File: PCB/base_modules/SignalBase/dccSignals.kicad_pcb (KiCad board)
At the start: 2 copper layers, 48 x 57.5 mm, 17 parts, among them J1 Screw_Terminal_01x02, J3 leds, J4 leds, J5 leds, J6 leds, SW1 SW_SPST, U1 ULN2003A, U2 ULN2003A

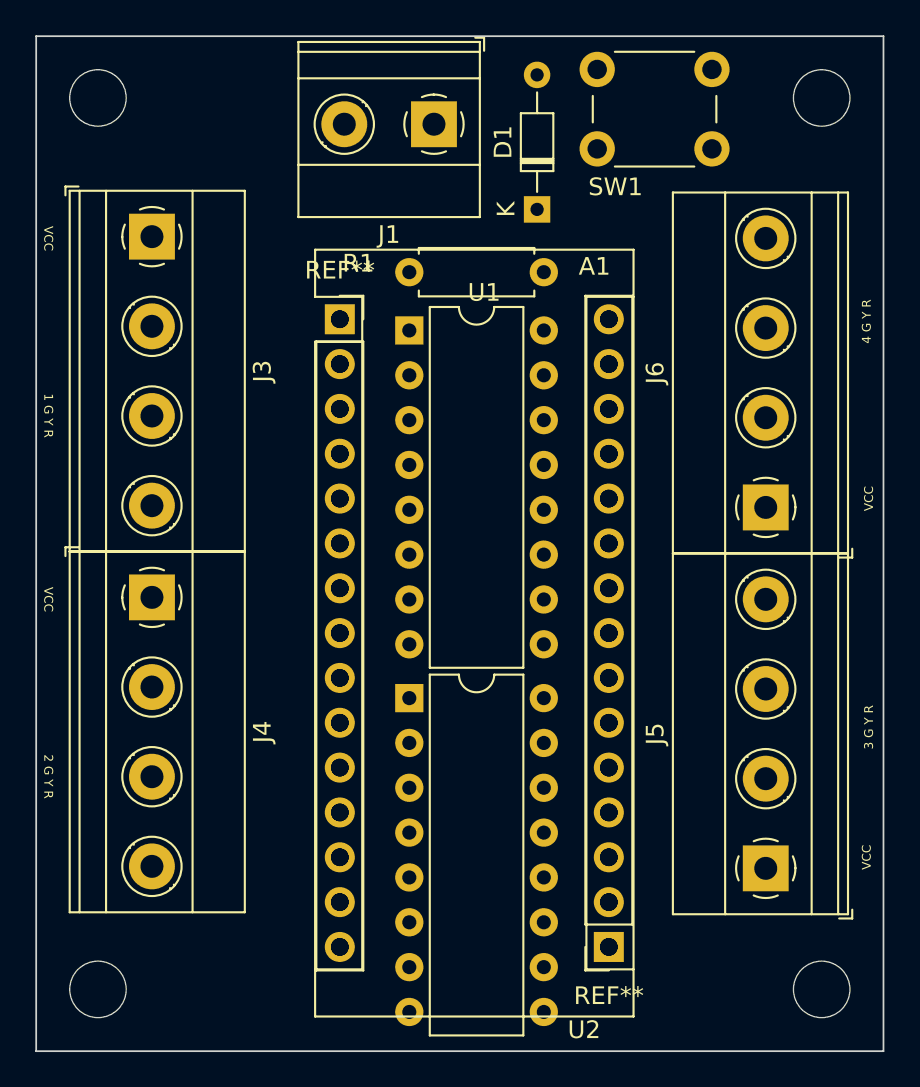
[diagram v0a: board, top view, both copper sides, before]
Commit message: routed signals PCB.
Was thinking to make a loconet block unit. Combined feedback, as well as
signal and ABC module. This would allow for automatic analog block
system for digital trains.
Also was thinking to make 2 separate blocks on 1 one pcb, provided if possible
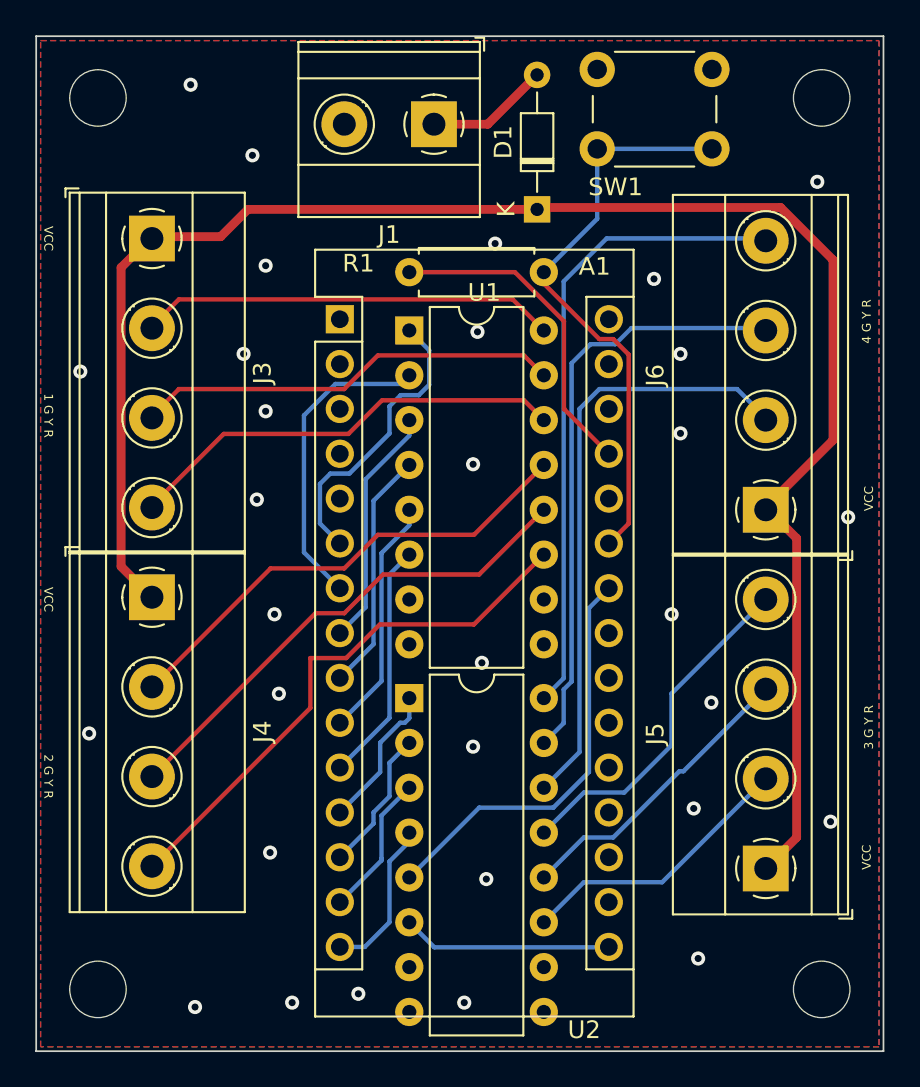
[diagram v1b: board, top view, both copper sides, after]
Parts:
- removed the REF** at (99.4, 133.1)
- removed the REF** at (84.2, 97.5)
- moved J6 0.14 mm to (108.3, 108.3)
- moved J3 0.11 mm to (73.6, 93.0)
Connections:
- U1 pad 9: VCC -> Net-(U1-Pad9)
- U2 pad 9: VCC -> Net-(U2-Pad9)
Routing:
- net VCC: track 0.00 -> 99.9 mm
- net /S4R: track 0.00 -> 36.5 mm
- net /S4G: track 0.00 -> 34.0 mm
- net /S4Y: track 0.00 -> 34.0 mm
- net Net-(A1-Pad25): track 0.00 -> 33.0 mm
- net /S2R: track 0.00 -> 31.2 mm
- net /S2Y: track 0.00 -> 28.5 mm
- net /S2G: track 0.00 -> 27.4 mm
- net /S1R: track 0.00 -> 25.1 mm
- net /S1Y: track 0.00 -> 24.1 mm
- net /S1G: track 0.00 -> 23.6 mm
- net /S3Y_IN: track 0.00 -> 23.5 mm
- net /S3R: track 0.00 -> 19.8 mm
- net +5V: track 0.00 -> 18.5 mm
- net /S1Y_IN: track 0.00 -> 17.5 mm
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- added copper zone on B.Cu, net GND
- added copper zone on F.Cu, net GND

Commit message: added detector pcb and signal pcb
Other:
- board text added: "V+"
- board text added: "V-"

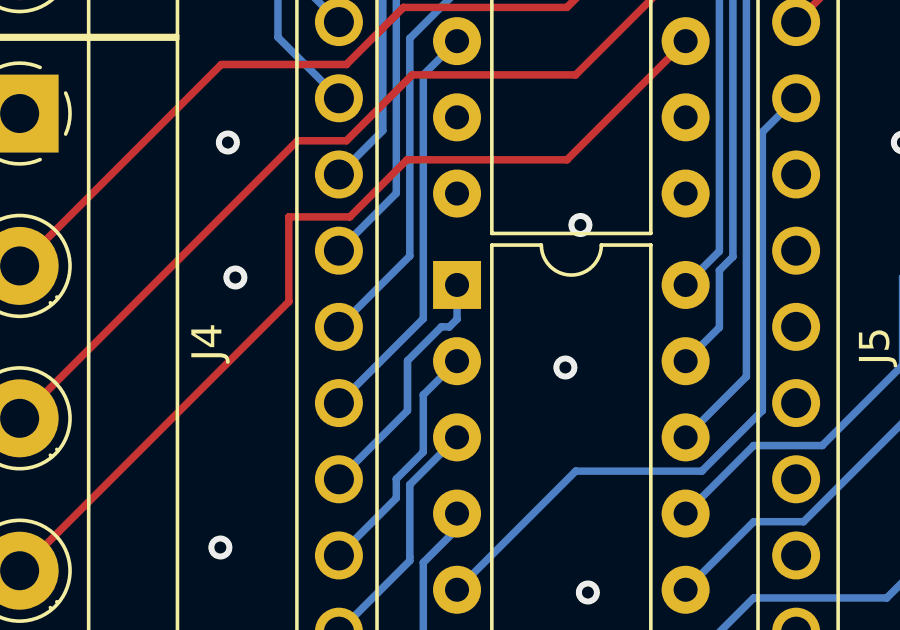
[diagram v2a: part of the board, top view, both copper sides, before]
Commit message: added gerber files in the release folder for all base units. The interfaces are not yet done
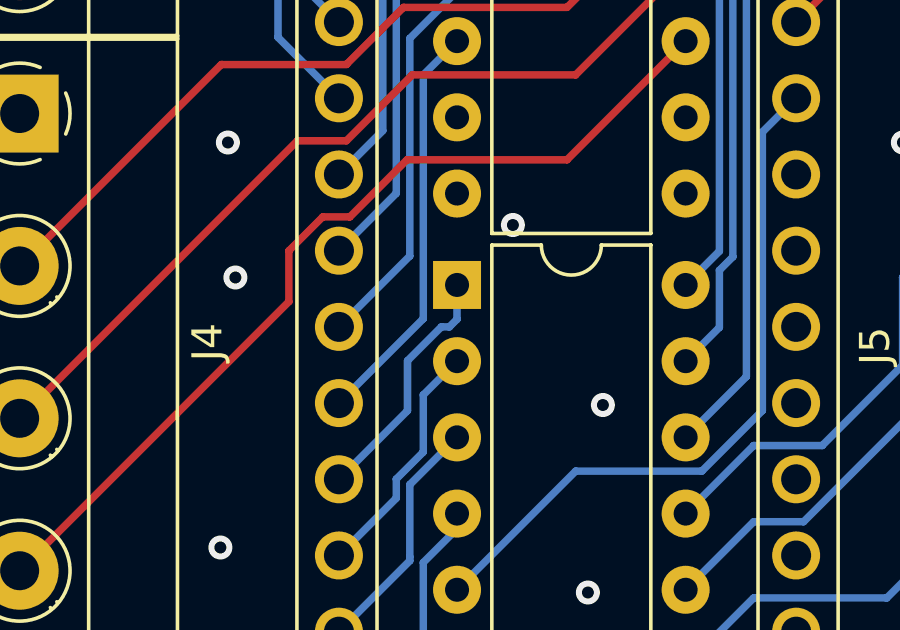
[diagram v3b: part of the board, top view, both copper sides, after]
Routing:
- net /S2R: track 31.2 -> 30.5 mm
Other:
- board text added: "Signal Base Module By Bas Knippels"
